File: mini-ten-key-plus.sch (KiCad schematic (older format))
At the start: 45 parts, among them SW0 SW_Push, U0 ProMicro

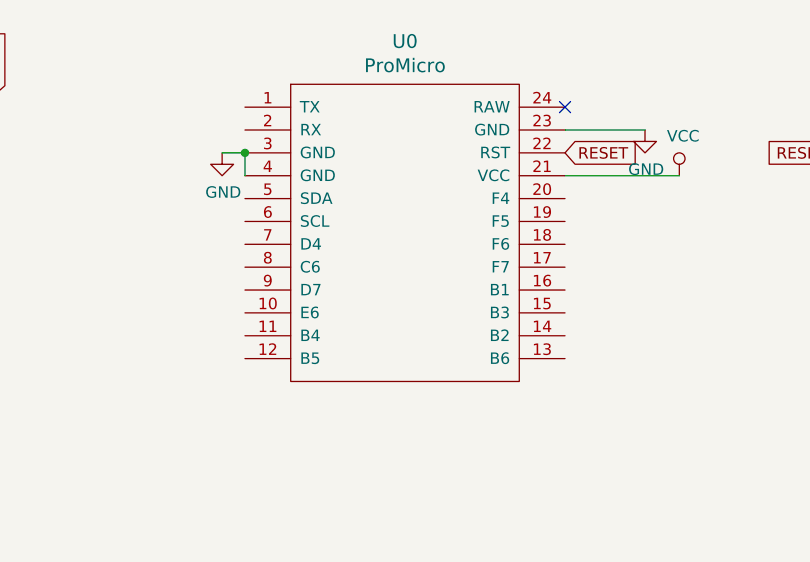
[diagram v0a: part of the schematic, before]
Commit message: Did practice col/row wiring
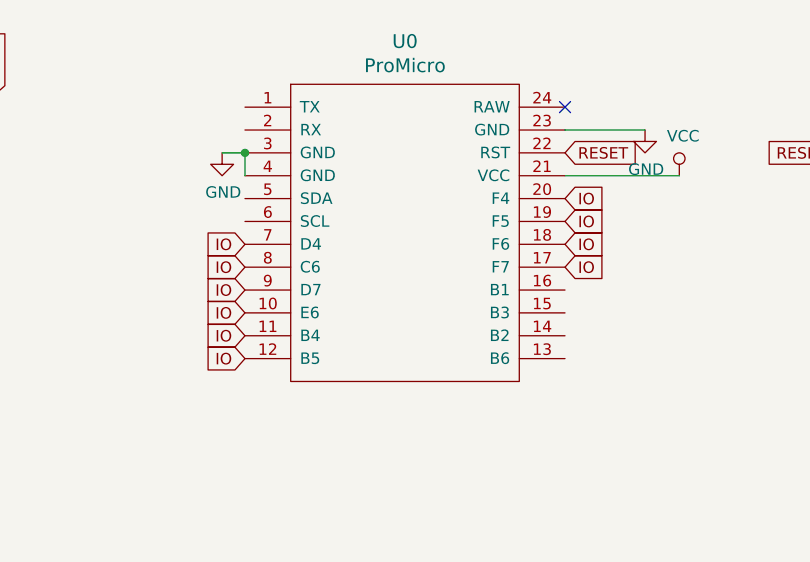
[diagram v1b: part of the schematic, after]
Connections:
- net IO: now reaches U0.10 (E6)
- net IO: now also U0.11 (B4), U0.12 (B5), U0.17 (F7), U0.18 (F6), U0.19 (F5), U0.20 (F4), U0.7 (D4), U0.8 (C6), U0.9 (D7)
